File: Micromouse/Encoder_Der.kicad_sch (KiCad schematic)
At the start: 6 parts, among them J11 AS5048_Der, U5 AS5048B-HTSP

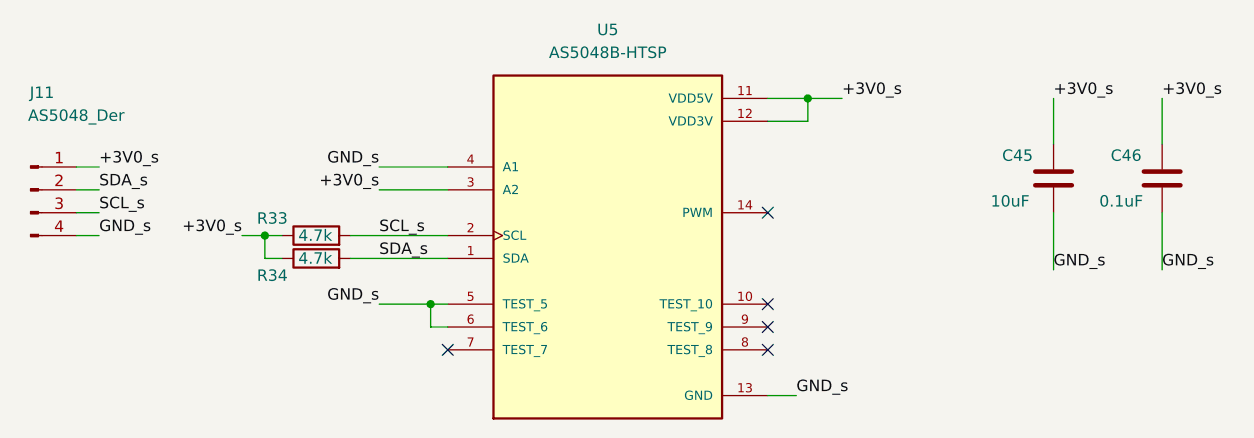
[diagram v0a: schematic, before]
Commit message: Red 3V0 cambiada a 3V3
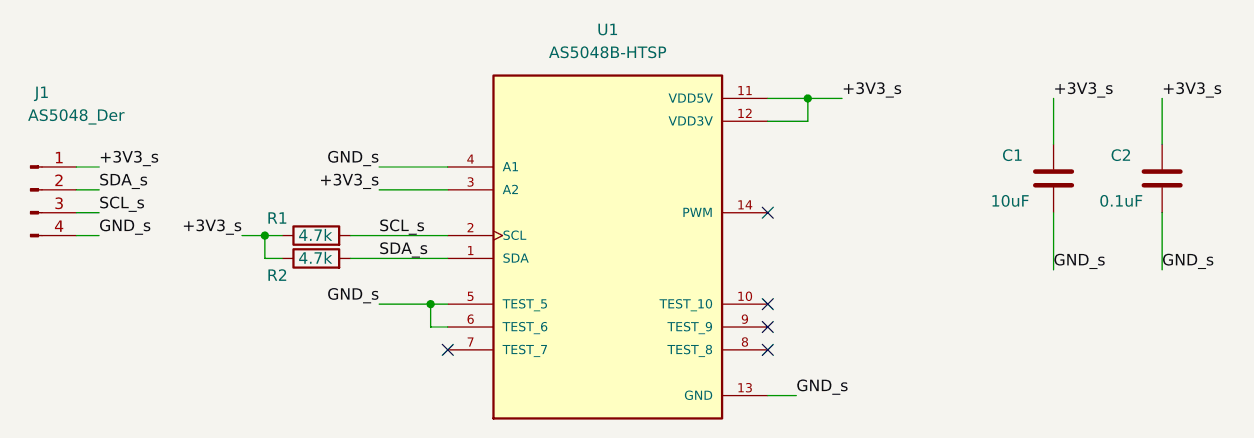
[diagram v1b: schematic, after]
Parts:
- renumbered C45 to C1, C46 to C2, J11 to J1, R33 to R1, R34 to R2, U5 to U1
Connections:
- net +3V0_s renamed +3V3_s
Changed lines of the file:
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@@
 		)
 	)
-	(label "+3V0_s"
+	(label "+3V3_s"
 		(at 169.545 81.915 0)
 		(effects
@@
 		)
 	)
-	(label "+3V0_s"
+	(label "+3V3_s"
 		(at 86.995 89.535 0)
 		(effects
@@
 		)
 	)
-	(label "+3V0_s"
+	(label "+3V3_s"
 		(at 118.11 92.075 180)
 		(effects
@@
 		)
 	)
-	(label "+3V0_s"
+	(label "+3V3_s"
 		(at 102.87 97.155 180)
 		(effects
@@
 		)
 	)
-	(label "+3V0_s"
+	(label "+3V3_s"
 		(at 205.105 81.915 0)
 		(effects
@@
 		)
 	)
-	(label "+3V0_s"
+	(label "+3V3_s"
 		(at 193.04 81.915 0)
 		(effects
@@
 		(on_board yes)
 		(dnp no)
-		(property "Reference" "R34"
+		(property "Reference" "R2"
 			(at 107.95 101.6 90)
 			(effects
@@
 				(path "/96b72c82-8e98-4b00-820e-849de0fa96c7/358c7740-1065-4f93-94de-62d9b382bca9"
 					(reference "R34")
+					(unit 1)
+				)
+			)
+			(project "Encoder_Der"
+				(path "/b451123f-ab77-45c6-ba5f-db48c0edb1c5"
+					(reference "R2")
 					(unit 1)
 				)
@@
 		(on_board yes)
 		(dnp no)
-		(property "Reference" "R33"
+		(property "Reference" "R1"
 			(at 107.95 95.25 90)
 			(effects
@@
 				(path "/96b72c82-8e98-4b00-820e-849de0fa96c7/358c7740-1065-4f93-94de-62d9b382bca9"
 					(reference "R33")
+					(unit 1)
+				)
+			)
+			(project "Encoder_Der"
+				(path "/b451123f-ab77-45c6-ba5f-db48c0edb1c5"
+					(reference "R1")
 					(unit 1)
 				)
@@
 		(on_board yes)
 		(dnp no)
-		(property "Reference" "C45"
+		(property "Reference" "C1"
 			(at 187.325 88.265 0)
 			(effects
@@
 				(path "/96b72c82-8e98-4b00-820e-849de0fa96c7/358c7740-1065-4f93-94de-62d9b382bca9"
 					(reference "C45")
+					(unit 1)
+				)
+			)
+			(project "Encoder_Der"
+				(path "/b451123f-ab77-45c6-ba5f-db48c0edb1c5"
+					(reference "C1")
 					(unit 1)
 				)
@@
 		(dnp no)
 		(fields_autoplaced yes)
-		(property "Reference" "U5"
+		(property "Reference" "U1"
 			(at 143.51 74.295 0)
 			(effects
@@
 				(path "/96b72c82-8e98-4b00-820e-849de0fa96c7/358c7740-1065-4f93-94de-62d9b382bca9"
 					(reference "U5")
+					(unit 1)
+				)
+			)
+			(project "Encoder_Der"
+				(path "/b451123f-ab77-45c6-ba5f-db48c0edb1c5"
+					(reference "U1")
 					(unit 1)
 				)
@@
 		(on_board yes)
 		(dnp no)
-		(property "Reference" "J11"
+		(property "Reference" "J1"
 			(at 80.645 81.28 0)
 			(effects
@@
 				(path "/96b72c82-8e98-4b00-820e-849de0fa96c7/358c7740-1065-4f93-94de-62d9b382bca9"
 					(reference "J11")
+					(unit 1)
+				)
+			)
+			(project "Encoder_Der"
+				(path "/b451123f-ab77-45c6-ba5f-db48c0edb1c5"
+					(reference "J1")
 					(unit 1)
 				)
@@
 		(on_board yes)
 		(dnp no)
-		(property "Reference" "C46"
+		(property "Reference" "C2"
 			(at 199.39 88.265 0)
 			(effects
@@
 				)
 			)
+			(project "Encoder_Der"
+				(path "/b451123f-ab77-45c6-ba5f-db48c0edb1c5"
+					(reference "C2")
+					(unit 1)
+				)
+			)
 		)
 	)
+	(sheet_instances
+		(path "/"
+			(page "1")
+		)
+	)
+	(embedded_fonts no)
 )
